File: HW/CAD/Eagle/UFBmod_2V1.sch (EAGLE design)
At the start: 200 parts, among them J1411 ABRACON_ARJE-0034, T0551 MMBT2222, U0501 MIDAS_MCCOG21605B6W-FPTLWI, U0601 MAX5217, U0701 AT86RF215-ZU, U0711 ASVTX-13-D-26.000MHZ-I05-T, U0811 PE4259, U0821 RFX1010, U0881 B39871B3440U410, U0911 FT232HL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

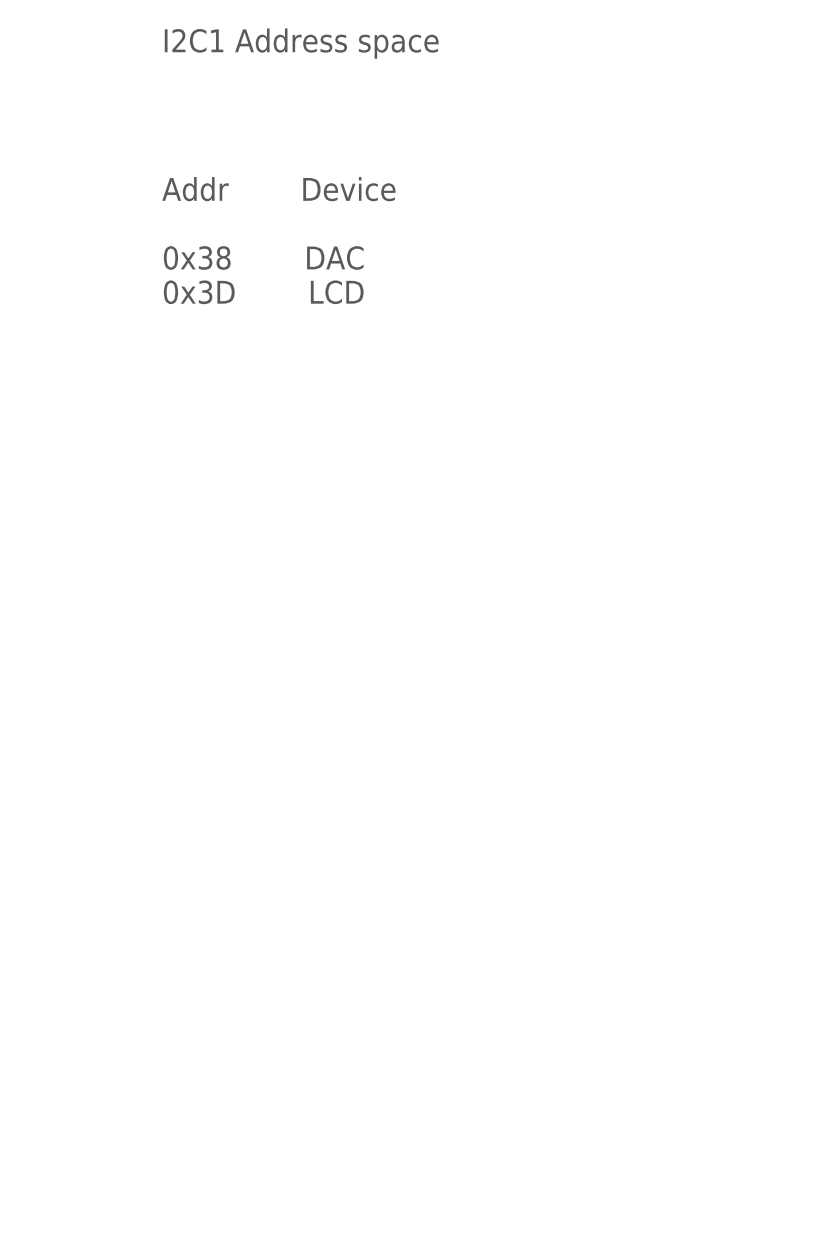
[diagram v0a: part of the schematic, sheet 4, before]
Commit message: HW - Eagle - V2.2 - reference voltage to be added, I2C address map fixed (V2.1 also)
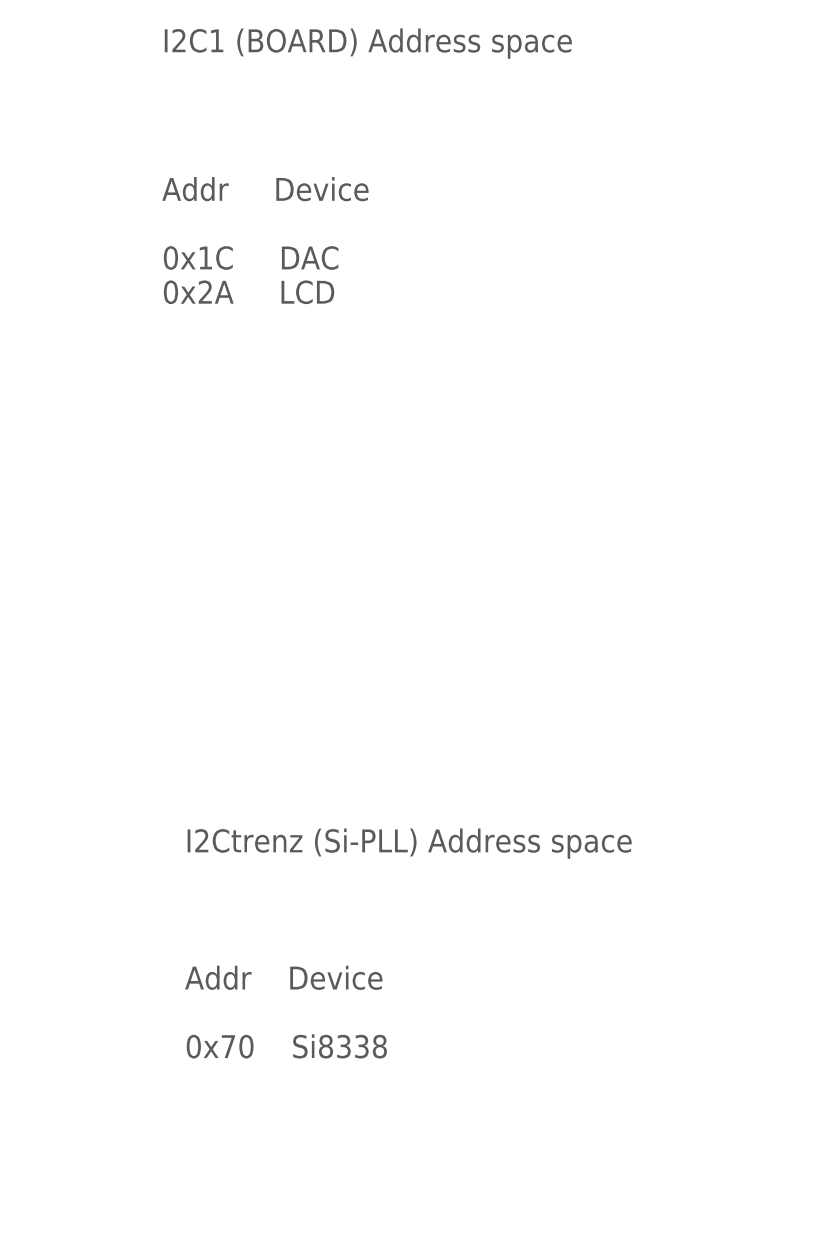
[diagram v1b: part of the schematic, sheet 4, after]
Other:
- note added: "Addr Device 0x1C DAC 0x2A LCD"
- note added: "Addr Device 0x70 Si8338"
- note added: "DAC for VCTCXO pull voltage I2C addr: 0x1C"
- note added: "Fix: connect Pin39 to Pin40."
- note added: "I2C LCD module I2C addr: 0x2A"
- note added: "I2C1 (BOARD) Address space"
- note added: "I2Ctrenz (Si-PLL) Address space"
- note removed: "Addr Device 0x38 DAC 0x3D LCD"
- note removed: "DAC for VCTCXO pull voltage I2C addr: 0x38"
- note removed: "I2C LCD module I2C addr: 0x3D"
- note removed: "I2C1 Address space"
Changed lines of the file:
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@@
 <plain>
 <text x="165.1" y="15.24" size="2.54" layer="97" ratio="15">I2C: Termination</text>
-<text x="149.86" y="134.62" size="2.54" layer="97" ratio="15">Addr        Device
-0x38        DAC
-0x3D        LCD</text>
 <text x="22.86" y="162.56" size="2.54" layer="97" ratio="15">I2C Termination</text>
-<text x="149.86" y="162.56" size="2.54" layer="97" ratio="15">I2C1 Address space</text>
+<text x="149.86" y="134.62" size="2.54" layer="97" ratio="15">Addr     Device
+0x1C     DAC
+0x2A     LCD</text>
+<text x="149.86" y="162.56" size="2.54" layer="97" ratio="15">I2C1 (BOARD) Address space</text>
+<text x="152.4" y="73.66" size="2.54" layer="97" ratio="15">I2Ctrenz (Si-PLL) Address space</text>
+<text x="152.4" y="50.8" size="2.54" layer="97" ratio="15">Addr    Device
+0x70    Si8338</text>
 </plain>
 <instances>
@@
 <description>I2C LCD</description>
 <plain>
-<text x="22.86" y="162.56" size="2.54" layer="97" ratio="15">I2C LCD module
-I2C addr: 0x3D</text>
+<text x="22.86" y="160.02" size="2.54" layer="97" ratio="15">I2C LCD module
+I2C addr: 0x2A</text>
 <text x="165.1" y="15.24" size="2.54" layer="97" ratio="15">I2C: LCD</text>
 </plain>
@@
 <text x="109.22" y="104.14" size="1.778" layer="97">Iq=80uA</text>
 <text x="22.86" y="160.02" size="2.54" layer="97" ratio="15">DAC for VCTCXO pull voltage
-I2C addr: 0x38</text>
+I2C addr: 0x1C</text>
 <text x="165.1" y="15.24" size="2.54" layer="97" ratio="15">I2C: DAC</text>
 </plain>
@@
 <text x="154.94" y="96.52" size="1.778" layer="94">out</text>
 <text x="154.94" y="93.98" size="1.778" layer="94">out</text>
+<text x="33.02" y="132.08" size="1.778" layer="97">Fix: connect Pin39 to Pin40.</text>
 </plain>
 <instances>
@@
 <wire x1="76.2" y1="137.16" x2="114.3" y2="137.16" width="0.1524" layer="91"/>
 <junction x="76.2" y="137.16"/>
-<wire x1="124.46" y1="38.1" x2="205.74" y2="38.1" width="0.1524" layer="91"/>
-<junction x="124.46" y="38.1"/>
-</segment>
-</net>
+</segment>
+</net>

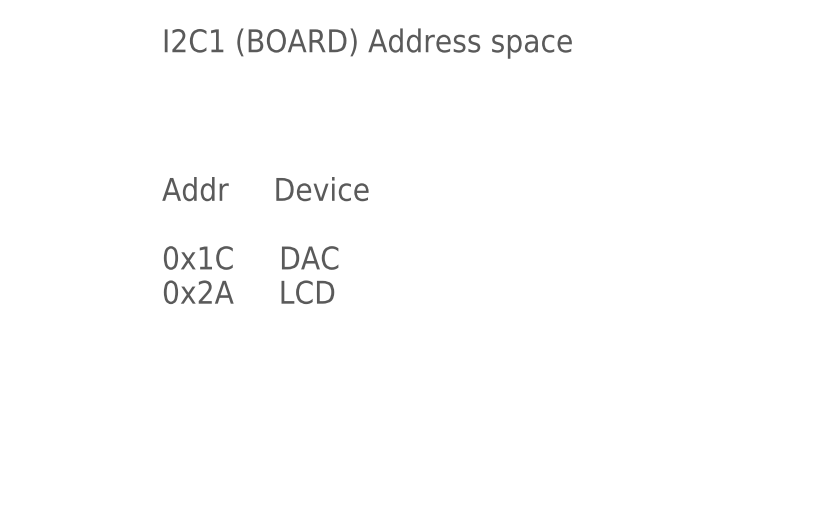
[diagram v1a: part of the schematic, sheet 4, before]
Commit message: HW - Eagle - V2.1 - I2C address map fixed again
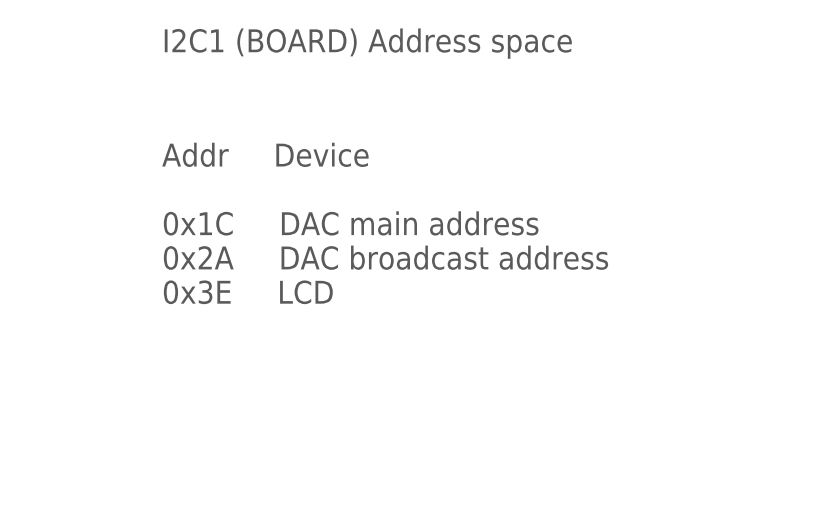
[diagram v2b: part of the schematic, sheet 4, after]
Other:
- note added: "Addr Device 0x1C DAC main address 0x2A DAC broadcast address 0x3E LCD"
- note added: "DAC for VCTCXO pull voltage I2C addr: 0x1C, I2C broadcast addr: 0x2A"
- note added: "I2C LCD module I2C addr: 0x3E"
- note removed: "Addr Device 0x1C DAC 0x2A LCD"
- note removed: "DAC for VCTCXO pull voltage I2C addr: 0x1C"
- note removed: "I2C LCD module I2C addr: 0x2A"
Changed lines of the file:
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@@
 <text x="22.86" y="162.56" size="2.54" layer="97" ratio="15">I2C Termination</text>
 <text x="149.86" y="134.62" size="2.54" layer="97" ratio="15">Addr     Device
-0x1C     DAC
-0x2A     LCD</text>
+0x1C     DAC main address
+0x2A     DAC broadcast address
+0x3E     LCD</text>
 <text x="149.86" y="162.56" size="2.54" layer="97" ratio="15">I2C1 (BOARD) Address space</text>
 <text x="152.4" y="73.66" size="2.54" layer="97" ratio="15">I2Ctrenz (Si-PLL) Address space</text>
@@
 <plain>
 <text x="22.86" y="160.02" size="2.54" layer="97" ratio="15">I2C LCD module
-I2C addr: 0x2A</text>
+I2C addr: 0x3E</text>
 <text x="165.1" y="15.24" size="2.54" layer="97" ratio="15">I2C: LCD</text>
 </plain>
@@
 <text x="109.22" y="104.14" size="1.778" layer="97">Iq=80uA</text>
 <text x="22.86" y="160.02" size="2.54" layer="97" ratio="15">DAC for VCTCXO pull voltage
-I2C addr: 0x1C</text>
+I2C addr: 0x1C, I2C broadcast addr: 0x2A</text>
 <text x="165.1" y="15.24" size="2.54" layer="97" ratio="15">I2C: DAC</text>
 </plain>

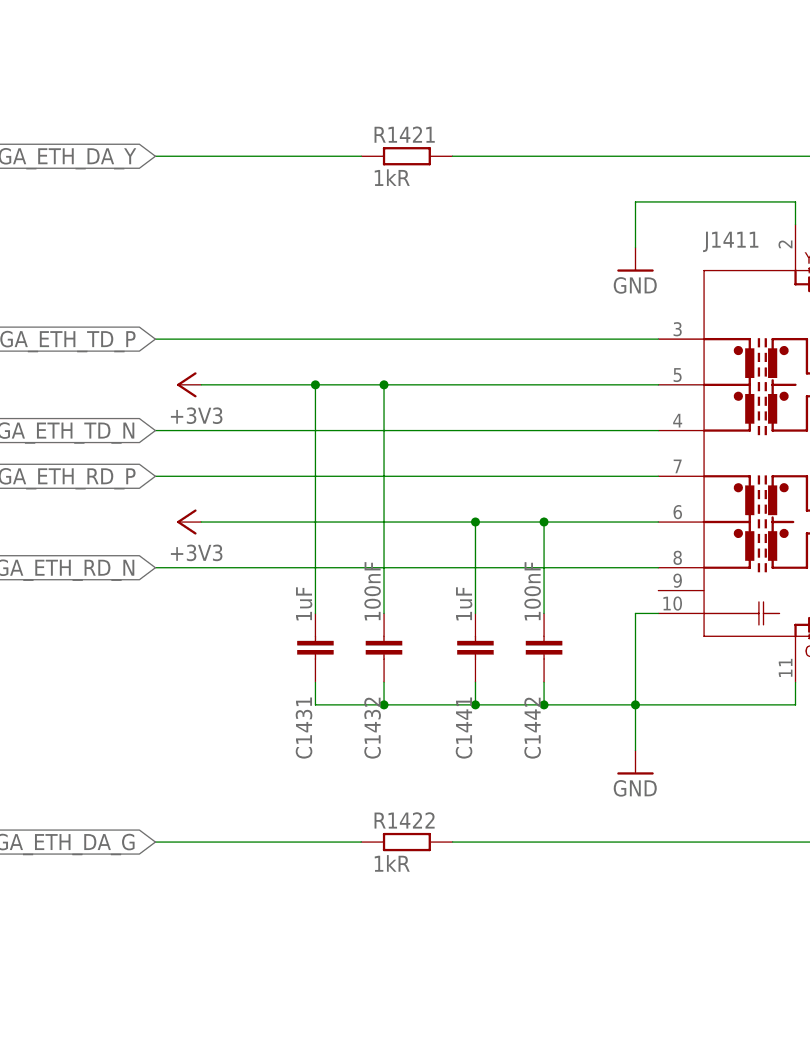
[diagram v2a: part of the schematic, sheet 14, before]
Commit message: HW - Eagle - V2.2 - Ethernet magnetics LED resistor values modified (V2.1 also)
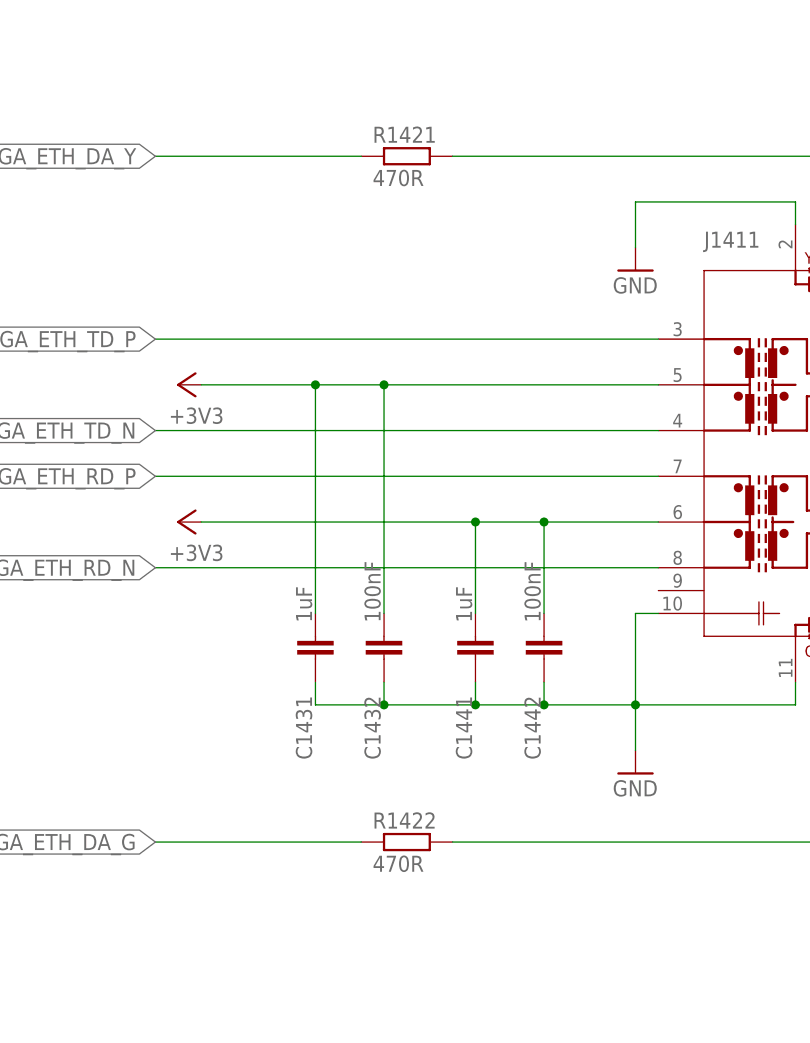
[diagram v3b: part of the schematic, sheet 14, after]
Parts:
- R1421, R1422: value 1kR -> 470R
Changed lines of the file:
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@@
 <part name="GND1412" library="df4iah_supply" deviceset="GND" device=""/>
 <part name="GND1413" library="df4iah_supply" deviceset="GND" device=""/>
-<part name="R1421" library="df4iah_rcl" deviceset="R-EU_" device="R0402" value="1kR"/>
-<part name="R1422" library="df4iah_rcl" deviceset="R-EU_" device="R0402" value="1kR"/>
+<part name="R1421" library="df4iah_rcl" deviceset="R-EU_" device="R0402" value="470R"/>
+<part name="R1422" library="df4iah_rcl" deviceset="R-EU_" device="R0402" value="470R"/>
 <part name="+3V3_1431" library="df4iah_supply" deviceset="+3V3" device=""/>
 <part name="+3V3_1441" library="df4iah_supply" deviceset="+3V3" device=""/>

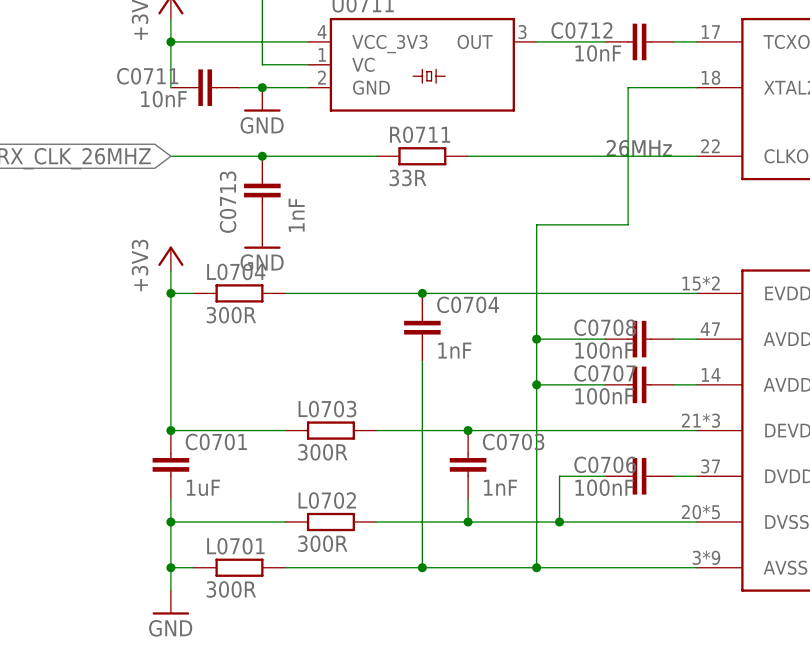
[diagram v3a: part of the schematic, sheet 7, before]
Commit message: HW - Eagle - V2.1 V2.2 - TRX corrections added
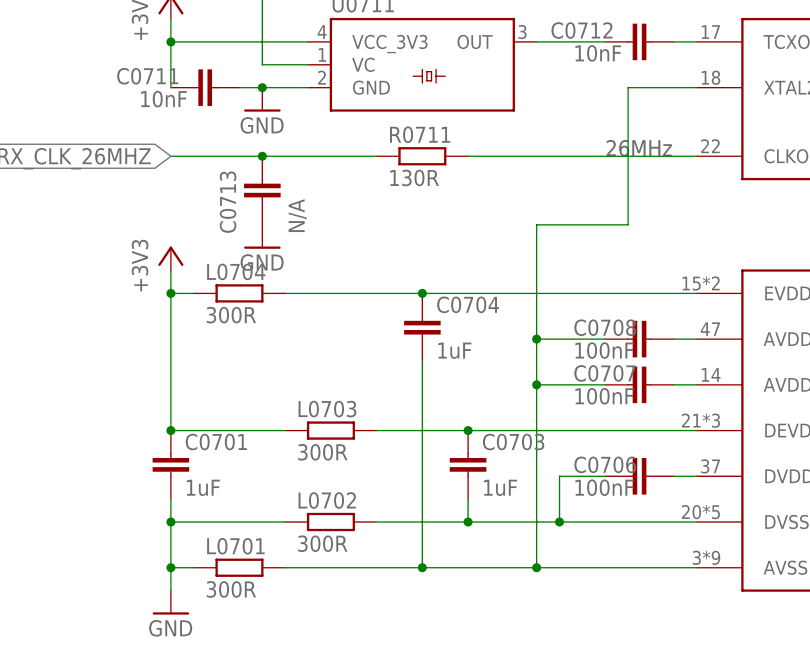
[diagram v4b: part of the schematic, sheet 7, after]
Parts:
- C0703, C0704: value 1nF -> 1uF
- C0713: value 1nF -> N/A
- R0711: value 33R -> 130R
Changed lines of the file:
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@@
 <part name="L0704" library="df4iah_rcl" deviceset="R-EU_" device="R1206" value="300R"/>
 <part name="+3V3_0701" library="df4iah_supply" deviceset="+3V3" device=""/>
-<part name="C0704" library="df4iah_rcl" deviceset="C-EU" device="C0402" value="1nF"/>
-<part name="C0703" library="df4iah_rcl" deviceset="C-EU" device="C0402" value="1nF"/>
+<part name="C0704" library="df4iah_rcl" deviceset="C-EU" device="C0402" value="1uF"/>
+<part name="C0703" library="df4iah_rcl" deviceset="C-EU" device="C0402" value="1uF"/>
 <part name="C0706" library="df4iah_rcl" deviceset="C-EU" device="C0402" value="100nF"/>
 <part name="C0708" library="df4iah_rcl" deviceset="C-EU" device="C0402" value="100nF"/>
@@
 <part name="S1321" library="df4iah_switch" deviceset="KSR223G_SMD_1POL" device=""/>
 <part name="R1321" library="df4iah_rcl" deviceset="R-EU_" device="R0402" value="1kR"/>
-<part name="R0711" library="df4iah_rcl" deviceset="R-EU_" device="R0402" value="33R"/>
+<part name="R0711" library="df4iah_rcl" deviceset="R-EU_" device="R0402" value="130R"/>
 <part name="C1321" library="df4iah_rcl" deviceset="C-EU" device="C0402" value="100nF"/>
 <part name="GND0001" library="df4iah_supply" deviceset="GND" device=""/>
-<part name="C0713" library="df4iah_rcl" deviceset="C-EU" device="C0402" value="1nF"/>
+<part name="C0713" library="df4iah_rcl" deviceset="C-EU" device="C0402" value="N/A"/>
 <part name="GND0712" library="df4iah_supply" deviceset="GND" device=""/>
 <part name="FPGA_EN1" library="df4iah_connector" deviceset="TP" device="B1,27"/>

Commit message: HW - Eagle - V2.1 V2.2 - TRX frontend pins configuration 1, not 2
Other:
- note added: "Config1 0: RX 1: TX"
- note added: "Config1 RX: H ON TX: L OFF"
- note added: "Config1 RX: L OFF TX: H ON"
- note removed: "Config2 0: OFF 1: ON"
- note removed: "Config2 0: RX 1: TX"
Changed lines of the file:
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@@
 <text x="22.86" y="162.56" size="2.54" layer="97" ratio="15">Front end: LNA &amp; PA for 868 MHz</text>
 <text x="165.1" y="15.24" size="2.54" layer="97" ratio="15">Front end 868 MHz</text>
-<text x="215.9" y="76.2" size="1.778" layer="97">Config2
+<text x="215.9" y="76.2" size="1.778" layer="97">Config1
 0: RX
 1: TX</text>
-<text x="134.62" y="20.32" size="1.778" layer="97">Config2
-0: OFF
-1: ON</text>
-<text x="149.86" y="20.32" size="1.778" layer="97">Config2
-0: RX
-1: TX</text>
+<text x="134.62" y="20.32" size="1.778" layer="97">Config1
+RX: H ON
+TX: L OFF</text>
+<text x="149.86" y="20.32" size="1.778" layer="97">Config1
+RX: L OFF
+TX: H ON</text>
 <text x="7.62" y="121.92" size="1.778" layer="97">X0891</text>
 <text x="7.62" y="40.64" size="1.778" layer="97">X0895</text>

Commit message: HW - Eagle - V2.1 V2.2 - TRX no 300R inductors at GND lines
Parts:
- L0701, L0702: value 300R -> 0R
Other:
- note added: "Replace L0701, L0702 by 0 Ohm bridges"
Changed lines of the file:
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@@
 <part name="FRAME_07" library="df4iah_frame" deviceset="A4L-LOC" device="" value="Holes"/>
 <part name="U0701" library="df4iah_rf" deviceset="AT86RF215" device="" value="AT86RF215-ZU"/>
-<part name="L0702" library="df4iah_rcl" deviceset="R-EU_" device="R1206" value="300R"/>
-<part name="L0701" library="df4iah_rcl" deviceset="R-EU_" device="R1206" value="300R"/>
+<part name="L0702" library="df4iah_rcl" deviceset="R-EU_" device="R1206" value="0R"/>
+<part name="L0701" library="df4iah_rcl" deviceset="R-EU_" device="R1206" value="0R"/>
 <part name="GND0701" library="df4iah_supply" deviceset="GND" device=""/>
 <part name="L0703" library="df4iah_rcl" deviceset="R-EU_" device="R1206" value="300R"/>
@@
 <text x="22.86" y="162.56" size="2.54" layer="97" ratio="15">Microchip Technologies AT86RF215</text>
 <text x="93.98" y="83.82" size="1.778" layer="97">26MHz</text>
+<text x="35.56" y="22.86" size="1.778" layer="97">Replace L0701, L0702 by 0 Ohm bridges</text>
 </plain>
 <instances>

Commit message: HW - Eagle - V2.1 V2.2 - RF power level remarks  added
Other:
- note added: "max. +1.3 dBm (TRX: +14 dBm set)"
- note added: "max. +14 dBm (TRX: +11 dBm set)"
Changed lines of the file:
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@@
 <text x="7.62" y="121.92" size="1.778" layer="97">X0891</text>
 <text x="7.62" y="40.64" size="1.778" layer="97">X0895</text>
+<text x="7.62" y="45.72" size="1.778" layer="97">max. +1.3 dBm (TRX: +14 dBm set)</text>
+<text x="7.62" y="132.08" size="1.778" layer="97">max. +14 dBm (TRX: +11 dBm set)</text>
 </plain>
 <instances>
